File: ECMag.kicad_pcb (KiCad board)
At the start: 2 copper layers, 110.5 x 59.7 mm, 51 parts, among them J1 Encoder Conn_01x12, J2 S. Magnético Conn_01x05, J3 Display Conn_01x04, J4 USB_B, J5 Barrel_Jack_SW, J6 RxTx Conn_01x04, K1 Tactil Switch B3F NA, K2 Tactil Switch B3F NA, K3 Tactil Switch B3F NA, K4 Tactil Switch B3F NA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

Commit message: Correcciones en los comentarios de la capa Dwgs
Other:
- rule pad_to_mask_clearance: 0.051 -> 0.075
- board text added: "Grilla 1,270 mm (50,00 mils) Diametro de pad o vía 0,80 mm Ancho de traza 0.450 mm Separación entre trazas 0,20 mm Separación entre traza y pad/vía 0.20 mm Antisoldante verde 3 (0.075 mm) Cobre de 2 Oz (0,07 mm) Sustrato FR4 1,60 mm Terminación ENIG Leyendas en blanco"
- board text removed: "Grilla 1,270 mm (50,00 mils) Diametro de pad o vía 0,80 mm Ancho de traza 0.450 mm Separación entre trazas 0,20 mm Separación entre traza y pad/vía 0.20 mm Cobre de 2 Oz (0,07 mm) Sustrato FR4 1,60 mm Terminación ENIG Leyendas en blanco Máscara antisoldante en verde"
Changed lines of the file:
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@@
     (36 B.SilkS user)
     (37 F.SilkS user)
-    (38 B.Mask user)
-    (39 F.Mask user hide)
+    (38 B.Mask user hide)
+    (39 F.Mask user)
     (40 Dwgs.User user)
     (41 Cmts.User user hide)
@@
     (pad_size 3.2 3.2)
     (pad_drill 3.2)
-    (pad_to_mask_clearance 0.051)
+    (pad_to_mask_clearance 0.075)
     (solder_mask_min_width 0.25)
     (aux_axis_origin 0 0)
@@
     (descr "28-lead though-hole mounted DIP package, row spacing 7.62 mm (300 mils)")
     (tags "THT DIP DIL PDIP 2.54mm 7.62mm 300mil")
+    (solder_mask_margin 0.075)
     (fp_text reference U1 (at 3.81 -2.54 90) (layer F.SilkS)
       (effects (font (size 1 1) (thickness 0.15)))
@@
     (descr "28-lead though-hole mounted DIP package, row spacing 7.62 mm (300 mils)")
     (tags "THT DIP DIL PDIP 2.54mm 7.62mm 300mil")
+    (solder_mask_margin 0.075)
     (fp_text reference U2 (at 3.81 -2.33 90) (layer F.SilkS)
       (effects (font (size 1 1) (thickness 0.15)))
@@
     (descr "USB B receptacle, Horizontal, through-hole, http://www.on-shore.com/wp-content/uploads/2015/09/usb-b1hsxx.pdf")
     (tags "USB-B receptacle horizontal through-hole")
+    (solder_mask_margin 0.075)
     (fp_text reference J4 (at 5.98 -7.97 90) (layer F.SilkS)
       (effects (font (size 1 1) (thickness 0.15)))
@@
     (descr "Wuerth electronics barrel jack connector (5.5mm outher diameter, inner diameter 2.05mm or 2.55mm depending on exact order number), See: http://katalog.we-online.de/em/datasheet/6941xx301002.pdf")
     (tags "connector barrel jack")
+    (solder_mask_margin 0.075)
     (fp_text reference J5 (at 7.62 5.08 90) (layer F.SilkS)
       (effects (font (size 1 1) (thickness 0.15)))
@@
     (effects (font (size 1 1) (thickness 0.15)) (justify left mirror))
   )
-  (gr_text "Grilla 1,270 mm (50,00 mils)\n\nDiametro de pad o vía 0,80 mm\nAncho de traza  0.450 mm\nSeparación entre trazas 0,20 mm\nSeparación entre traza y pad/vía 0.20 mm\nCobre de 2 Oz (0,07 mm)\nSustrato FR4  1,60 mm\nTerminación ENIG\nLeyendas en blanco\nMáscara antisoldante en verde" (at 90.7542 38.5064) (layer Dwgs.User)
+  (gr_text "Grilla 1,270 mm (50,00 mils)\n\nDiametro de pad o vía 0,80 mm\nAncho de traza  0.450 mm\nSeparación entre trazas 0,20 mm\nSeparación entre traza y pad/vía 0.20 mm\nAntisoldante verde 3 (0.075 mm)\nCobre de 2 Oz (0,07 mm)\nSustrato FR4  1,60 mm\nTerminación ENIG\nLeyendas en blanco" (at 90.7542 38.5064) (layer Dwgs.User)
     (effects (font (size 2.5 3.5) (thickness 0.2)) (justify left))
   )

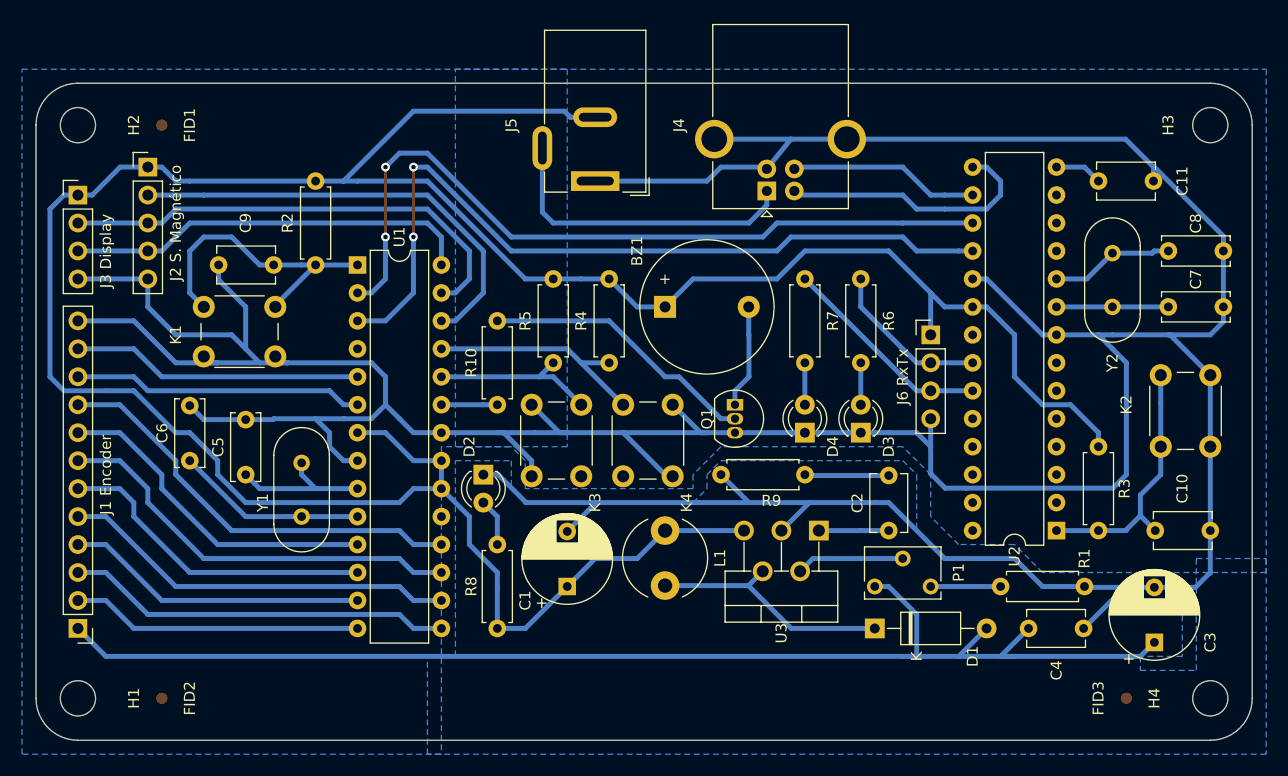
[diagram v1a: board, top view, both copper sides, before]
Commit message: Eliminación de Tracks superfluos tapados por otros tracks
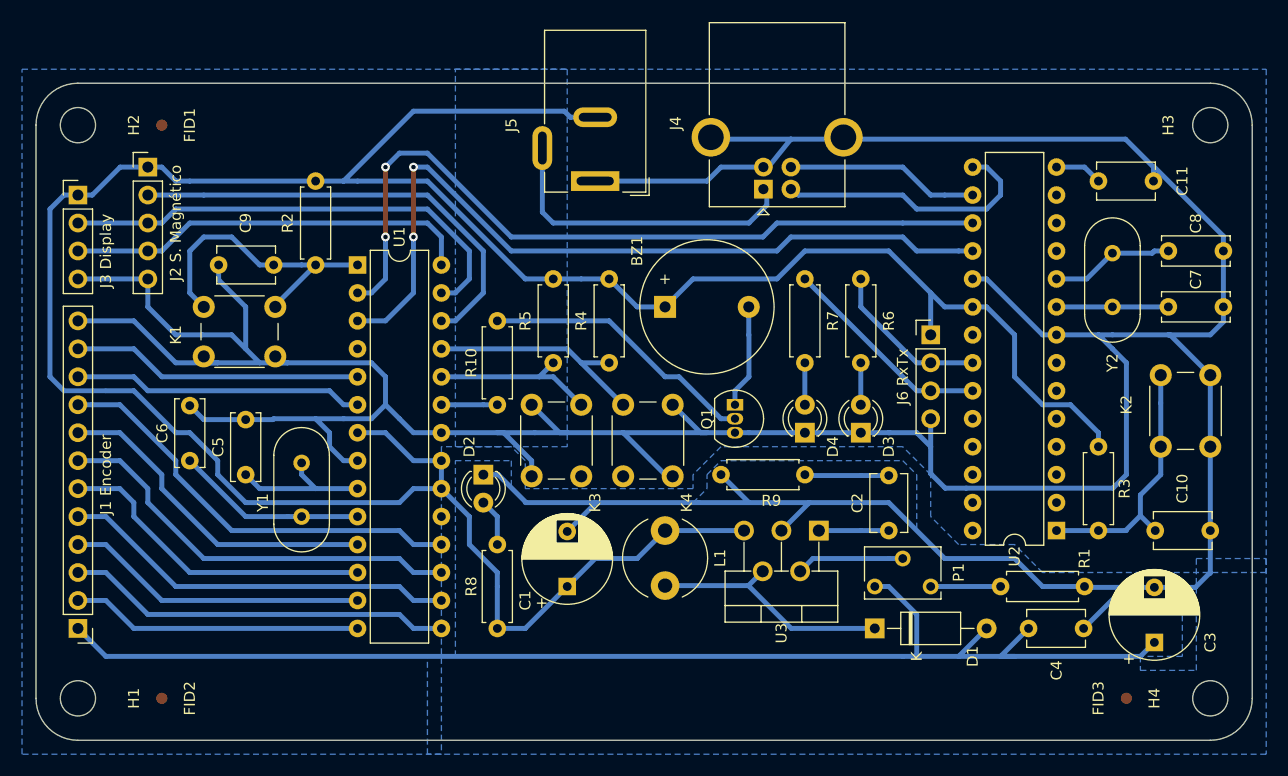
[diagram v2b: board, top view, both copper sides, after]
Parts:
- moved J4 0.35 mm to (158.8, 80.7)
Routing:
- net GND: track 414.7 -> 413.4 mm
- net +5V: track 254.2 -> 253.0 mm
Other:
- rule trace_min: 0.2 -> 0.45

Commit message: 1.- Reemplaxado K por Sw en el esquemático.
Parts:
- J1: renamed from J1 Encoder
- J2: renamed from J2 S. Magnético
- J3: renamed from J3 Display
- J6: renamed from J6 RxTx
- renumbered K1 to Sw1, K2 to Sw2, K3 to Sw3, K4 to Sw4
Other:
- net class Default: clearance 0.2 -> 0.25; via_dia 0.8 -> 0.9; via_drill 0.4 -> 0.45
- net class Potencia: clearance 0.2 -> 0.25; via_dia 0.8 -> 0.9; via_drill 0.4 -> 0.45
- net class Senhal: clearance 0.2 -> 0.25; via_dia 0.8 -> 0.9; via_drill 0.4 -> 0.45
- rule trace_clearance: 0.2 -> 0.25
- rule via_min_drill: 0.3 -> 0.45
- rule via_min_size: 0.4 -> 0.45
- board text added: "Diseñado en la Ciudad Autónoma de Buenos Aires. Industria Argentina."
- board text added: "Grilla 1,270 mm (50,00 mils) Diametro de pad o vía 0,90 mm Ancho de traza 0.450 mm Separación entre trazas 0,25 mm Separación entre traza y pad/vía 0.25 mm Antisoldante verde 3 (0.075 mm) Cobre de 2 Oz (0,07 mm) Sustrato FR4 1,60 mm Terminación ENIG Leyendas en blanco"
- board text added: "Version: 1.0 Rev: 2"
- board text removed: "Grilla 1,270 mm (50,00 mils) Diametro de pad o vía 0,80 mm Ancho de traza 0.450 mm Separación entre trazas 0,20 mm Separación entre traza y pad/vía 0.20 mm Antisoldante verde 3 (0.075 mm) Cobre de 2 Oz (0,07 mm) Sustrato FR4 1,60 mm Terminación ENIG Leyendas en blanco"
- board text removed: "Version: 1.0 Rev: 1"
